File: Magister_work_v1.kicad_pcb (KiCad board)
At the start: 4 copper layers, 100 x 100 mm, 83 parts, among them J1 Conn_01x04_Pin, J10 Conn_01x02_Pin, J2 Conn_01x03_Pin, J3 Conn_01x03_Pin, J4 Conn_01x03_Pin, J5 Conn_01x03_Pin, J6 Conn_01x04_Pin, J7 Conn_01x04_Pin, J8 Conn_01x06_Pin, J9 Conn_01x02_Pin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

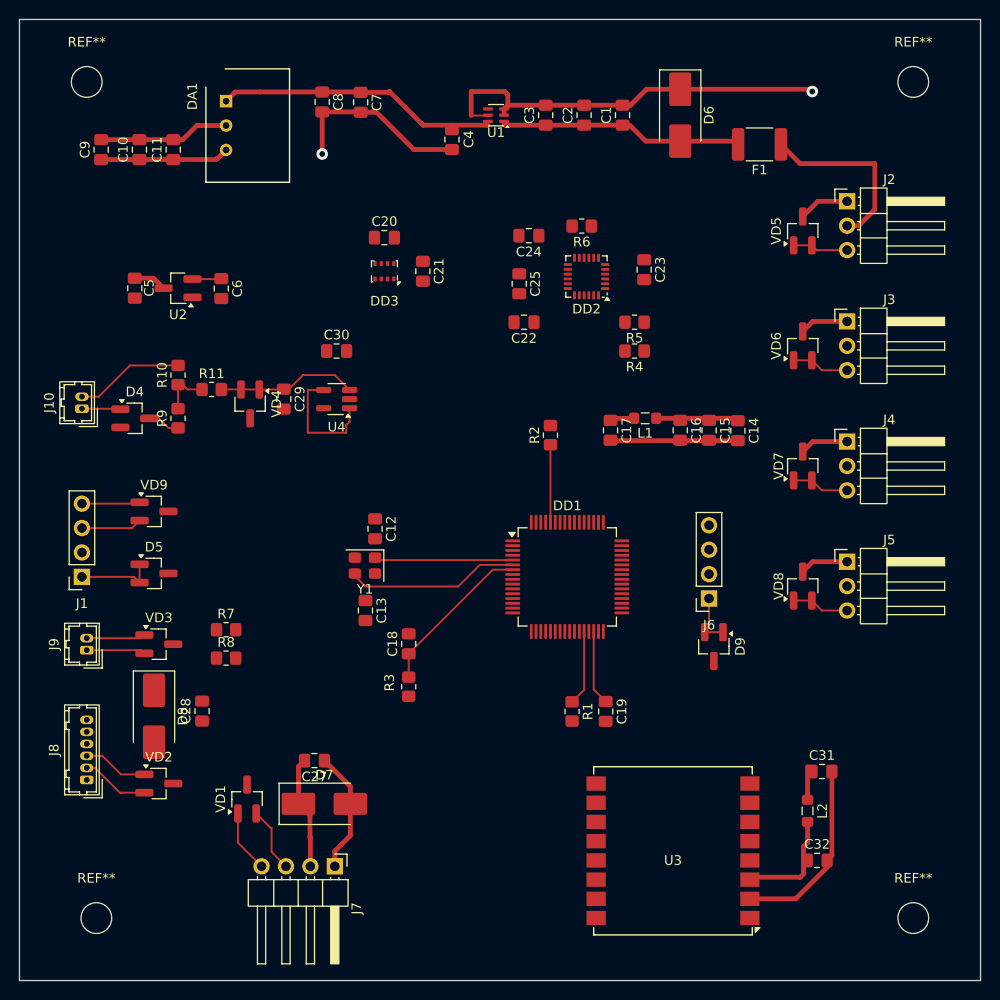
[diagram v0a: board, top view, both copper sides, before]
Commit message: feat: added power lines for MCU
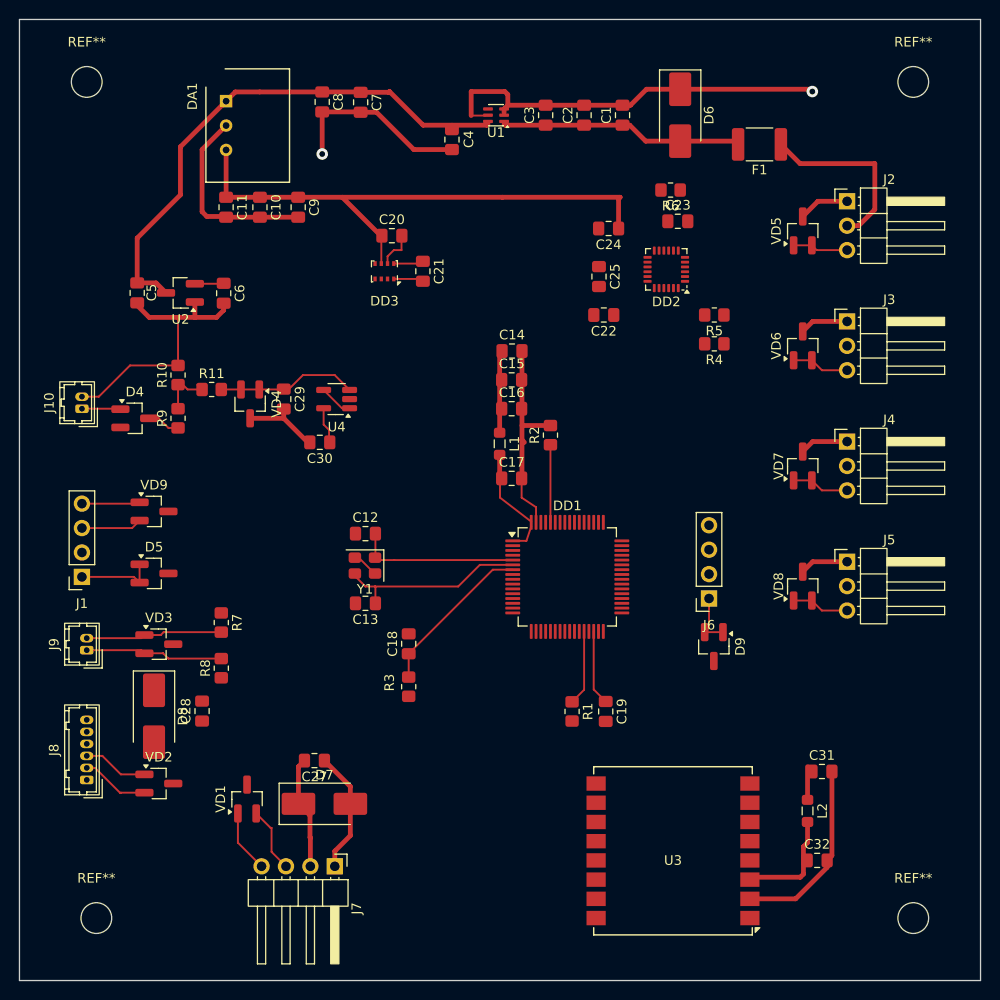
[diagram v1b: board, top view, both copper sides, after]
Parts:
- moved C14 24.9 mm to (76.2, 59.5), turned to 0 degrees
- moved C9 21.4 mm to (54.0, 44.5), turned to -90 degrees
- moved C15 21.2 mm to (76.2, 62.5), turned to 0 degrees
- moved C16 17.7 mm to (76.2, 65.5), turned to 0 degrees
- moved L1 15.4 mm to (75.0, 69.2), turned to -90 degrees
- moved C10 13.9 mm to (50.0, 44.5), turned to -90 degrees
- moved C17 11.4 mm to (76.2, 72.8), turned to 0 degrees
- moved R6 9.98 mm to (92.8, 42.8)
- moved C30 9.66 mm to (56.2, 69.0), turned to 180 degrees
- moved C22 8.33 mm to (85.8, 55.8)
- moved C24 8.33 mm to (86.3, 46.8)
- moved C25 8.33 mm to (85.3, 51.8)
- moved DD2 8.33 mm to (92.3, 51.0)
- moved R4 8.33 mm to (97.3, 58.8)
- moved R5 8.33 mm to (97.3, 55.8)
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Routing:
- net GND: track 227.1 -> 272.5 mm
- net +3V3D: track 25.5 -> 70.0 mm
- net +5V: track 45.4 -> 68.2 mm
- net BAT_CTRL: track 12.8 -> 3.49 mm
- net BN_880_SDA: track 6.13 -> 14.4 mm
- net BN_880_SCL: track 6.13 -> 14.3 mm
- net +3V3A: track 3.02 -> 9.93 mm
- net Net-(DD1-PH0): track 14.4 -> 16.9 mm
- net Net-(DD1-PH1): track 18.1 -> 19.8 mm

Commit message: fix: fix bug with locked hole
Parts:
- removed REF** (x4): MountingHole_3.2mm_M3, MountingHole:MountingHole_3.2mm_M3
- added ?: , , F.Cu at (118.0, 31.5)
- added ?: , , F.Cu at (118.0, 118.5)
- added ?: , , F.Cu at (32.0, 31.5)
- added ?: , , F.Cu at (33.0, 118.5)
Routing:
- net GND: track 272.5 -> 286.2 mm
- net +5V: track 68.2 -> 76.8 mm, vias 0 -> 1

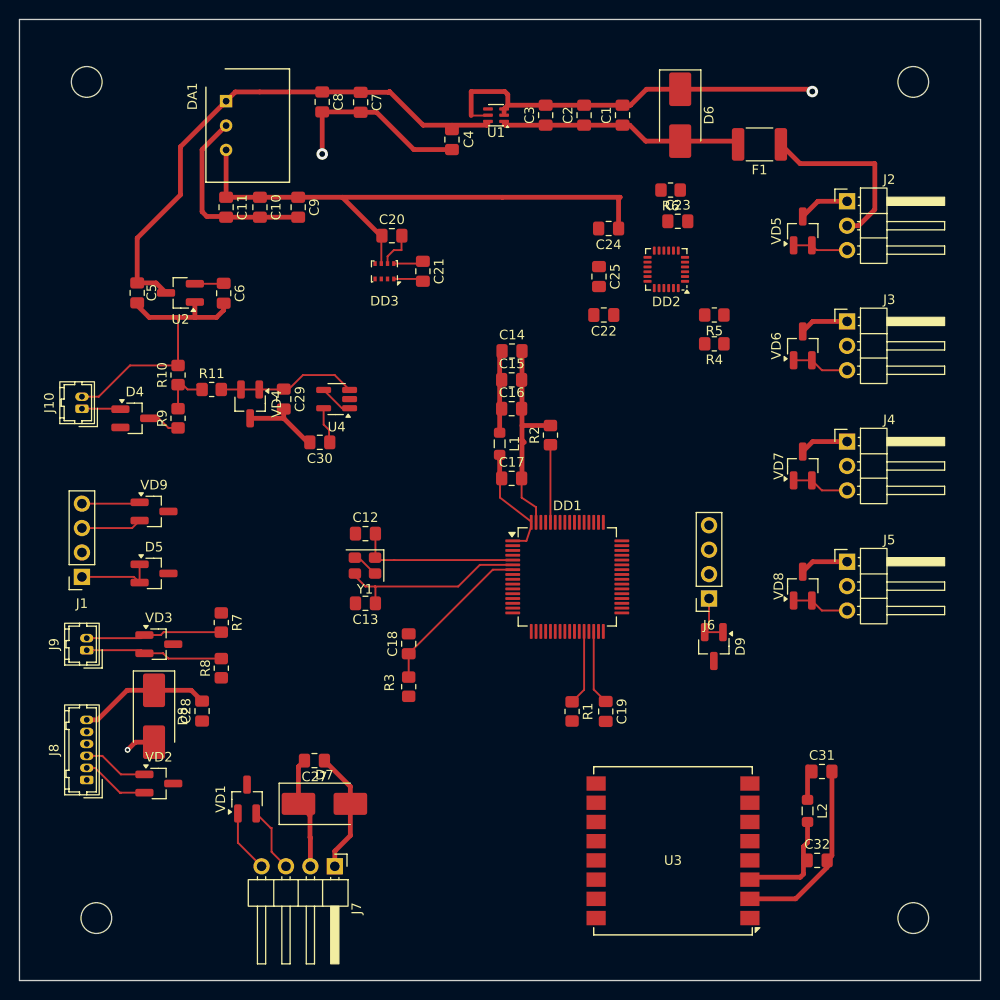
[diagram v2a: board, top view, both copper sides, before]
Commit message: feat: added MPU and PWM line
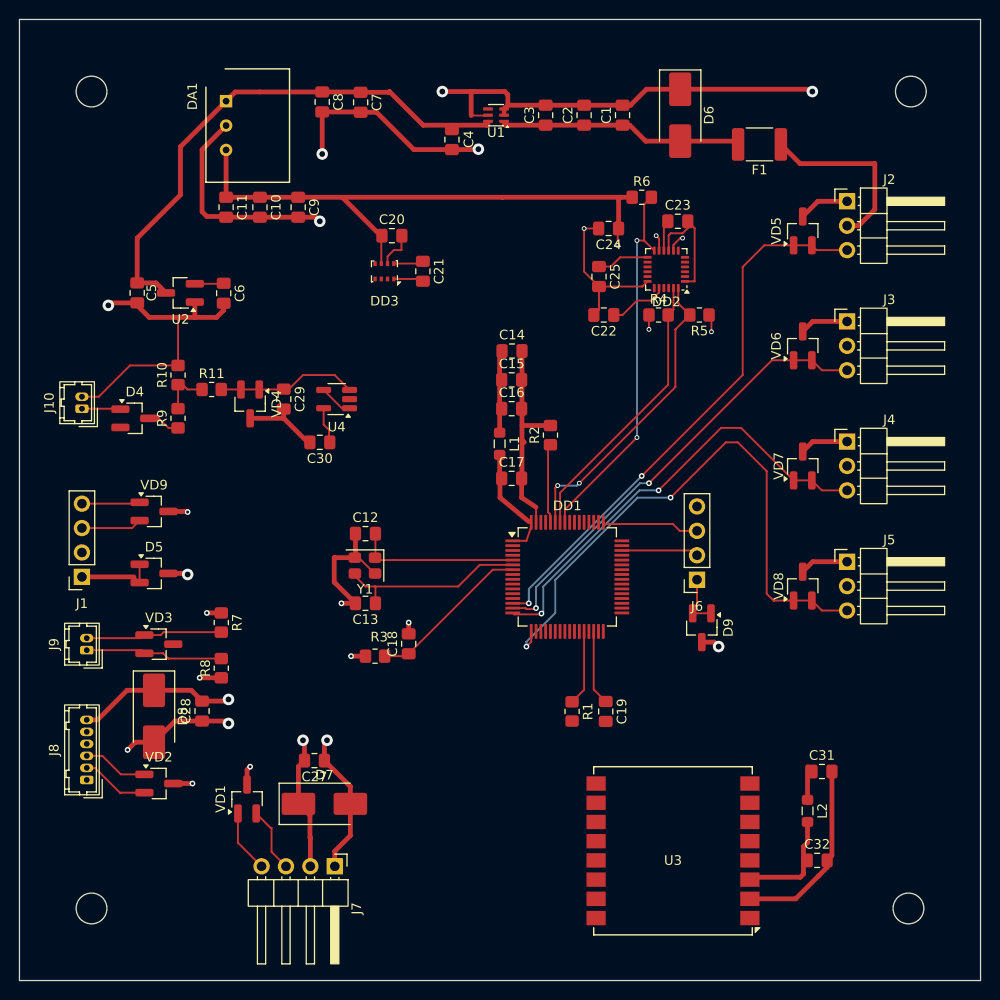
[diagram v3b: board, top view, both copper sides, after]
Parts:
- moved R4 6.53 mm to (91.5, 55.8), turned to 0 degrees
- moved R3 4.73 mm to (62.0, 91.2), turned to 0 degrees
- moved R6 3.09 mm to (89.8, 43.5), turned to 0 degrees
- moved D9 2.32 mm to (96.0, 88.3)
- moved J6 2.32 mm to (95.5, 83.3)
- moved R5 1.55 mm to (95.8, 55.8)
- moved ? 1.12 mm to (117.5, 117.5)
- moved ? 1.12 mm to (32.5, 32.5)
- moved ? 1.12 mm to (32.5, 117.5)
- moved ? 1.03 mm to (117.8, 32.5)
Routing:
- net GND: track 286.2 -> 395.7 mm, vias 2 -> 15
- net PWM4: track 6.00 -> 61.0 mm, vias 0 -> 2
- net PWM1: track 5.77 -> 57.9 mm, vias 0 -> 2
- net PWM2: track 6.00 -> 47.3 mm, vias 0 -> 2
- net PWM3: track 6.00 -> 47.1 mm, vias 0 -> 2
- net INT_MPU6050: track 0.00 -> 39.5 mm, vias 0 -> 2
- net +3V3D: track 70.0 -> 108.4 mm, vias 0 -> 8
- net SDA_MPU6050: track 0.00 -> 31.8 mm, vias 0 -> 2
- net SCL_MPU6050: track 0.00 -> 29.3 mm
- net +5V: track 76.8 -> 89.8 mm, vias 1 -> 4
- net Net-(DD1-PA14): track 0.00 -> 10.1 mm
- net Net-(DD1-PA13): track 0.00 -> 8.03 mm
- net Net-(DD2-CPOUT): track 0.00 -> 6.14 mm
- net +3V3A: track 9.93 -> 15.4 mm
- net Net-(DD2-REGOUT): track 0.00 -> 3.22 mm

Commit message: feat: added mani lines for GND
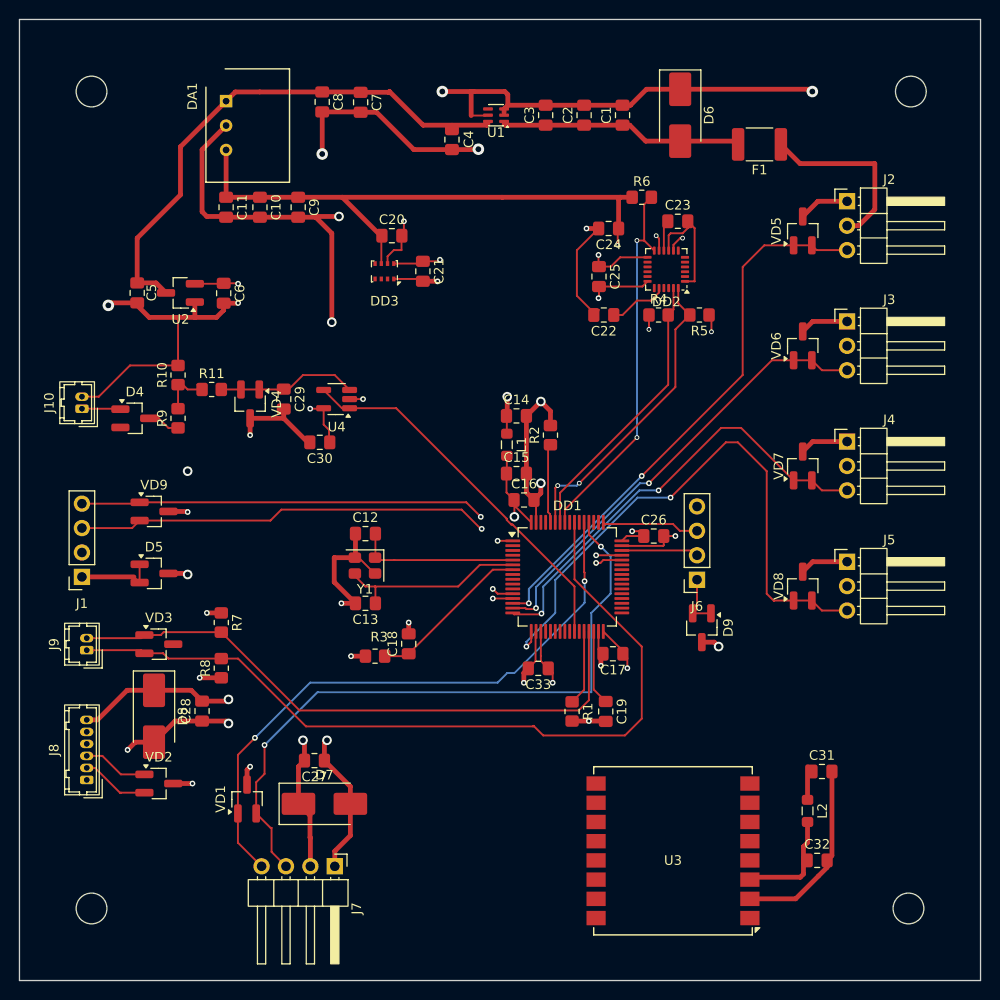
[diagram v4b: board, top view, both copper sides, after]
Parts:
- added C26: 0.1u, Capacitor_SMD:C_0805_2012Metric_Pad1.18x1.45mm_HandSolder, F.Cu at (91.0, 78.8)
- added C33: 0.1u, Capacitor_SMD:C_0805_2012Metric_Pad1.18x1.45mm_HandSolder, F.Cu at (79.0, 92.5)
- moved C17 21.1 mm to (86.8, 91.0), turned to 180 degrees
- moved C15 9.76 mm to (76.7, 72.2)
- moved C16 9.59 mm to (77.5, 75.0)
- moved C14 6.77 mm to (76.7, 66.2)
- moved L1 0.76 mm to (75.7, 69.2)
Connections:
- C15 pad 1: +3V3D -> +3V3_MCU
- C16 pad 1: +3V3D -> +3V3_MCU
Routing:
- net GND: track 395.7 -> 655.5 mm, vias 15 -> 30
- net +3V3A: track 15.4 -> 123.1 mm, vias 0 -> 5
- net +3V3_MCU: track 2.71 -> 76.9 mm, vias 0 -> 5
- net BN_880_SDA: track 14.4 -> 85.5 mm
- net HC_trigger: track 6.84 -> 70.0 mm, vias 0 -> 2
- net HC_echo: track 6.52 -> 63.6 mm, vias 0 -> 2
- net TX_debug: track 6.32 -> 59.4 mm, vias 0 -> 2
- net RX_debug: track 6.06 -> 58.5 mm, vias 0 -> 2
- net BN_880_SCL: track 14.3 -> 63.5 mm
- net BAT_CTRL: track 3.49 -> 39.3 mm
- net +3V3D: track 108.4 -> 103.7 mm, vias 8 -> 9

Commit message: feat: add zone for 3v3D power
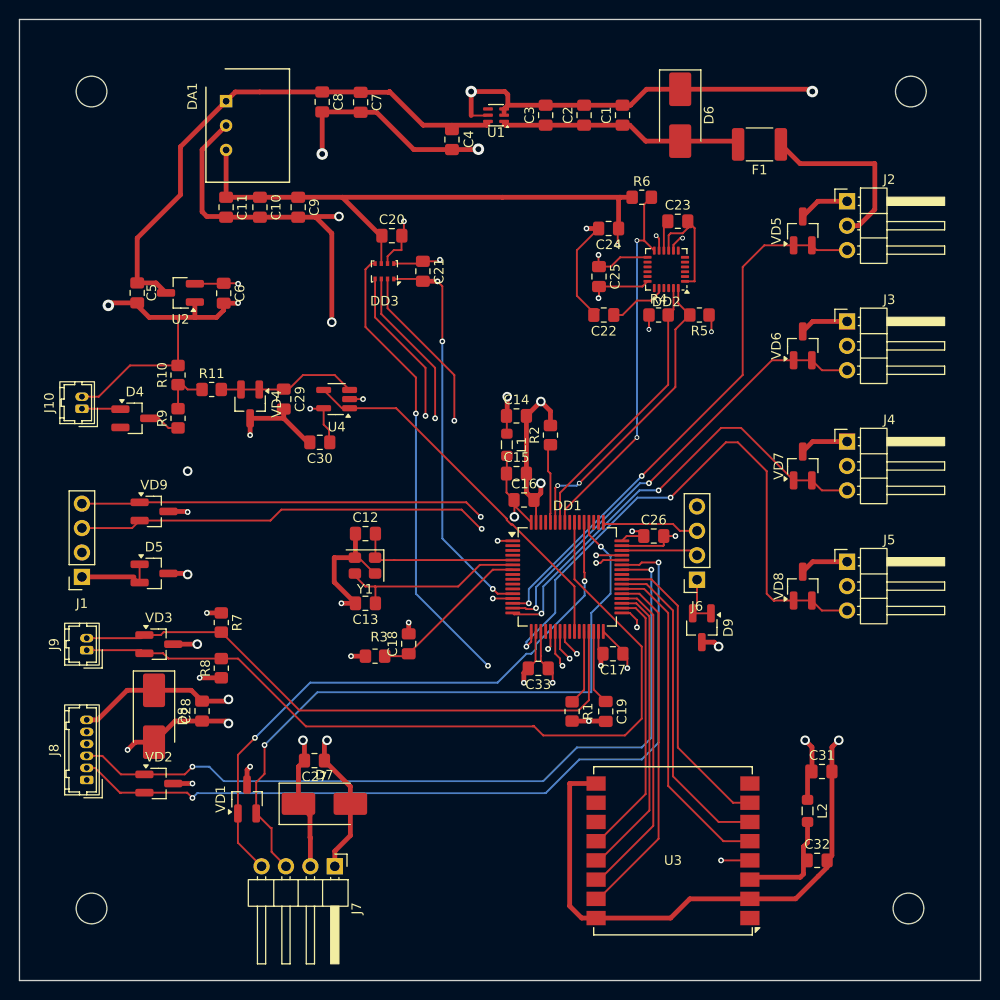
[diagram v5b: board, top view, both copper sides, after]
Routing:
- net +5V: track 89.8 -> 183.9 mm
- net BN_880_TX: track 7.11 -> 85.9 mm, vias 0 -> 2
- net BN_880_RX: track 6.80 -> 82.9 mm, vias 0 -> 2
- net GND: track 655.5 -> 727.1 mm, vias 30 -> 33
- net SDO_BMP280: track 0.00 -> 64.1 mm, vias 0 -> 3
- net SDI_BMP280: track 0.00 -> 53.8 mm, vias 0 -> 2
- net CSB_BMP280: track 0.00 -> 53.2 mm, vias 0 -> 2
- net SCK_BMP280: track 0.00 -> 51.2 mm, vias 0 -> 2
- net +3V3_MCU: track 76.9 -> 27.4 mm
- net SS_LoRa: track 0.00 -> 37.2 mm
- net DIO0_LoRa: track 0.00 -> 34.7 mm
- net MOSI_LoRa: track 0.00 -> 34.2 mm
- net DIO1_LoRa: track 0.00 -> 33.7 mm
- net Reset_LoRa: track 0.00 -> 33.5 mm, vias 0 -> 2
- net DIO2_LoRa: track 0.00 -> 31.6 mm
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- added copper zone on In1.Cu, net +3V3D
- added copper zone on In1.Cu, net +3V3_MCU
- added copper zone on In1.Cu, net +5V

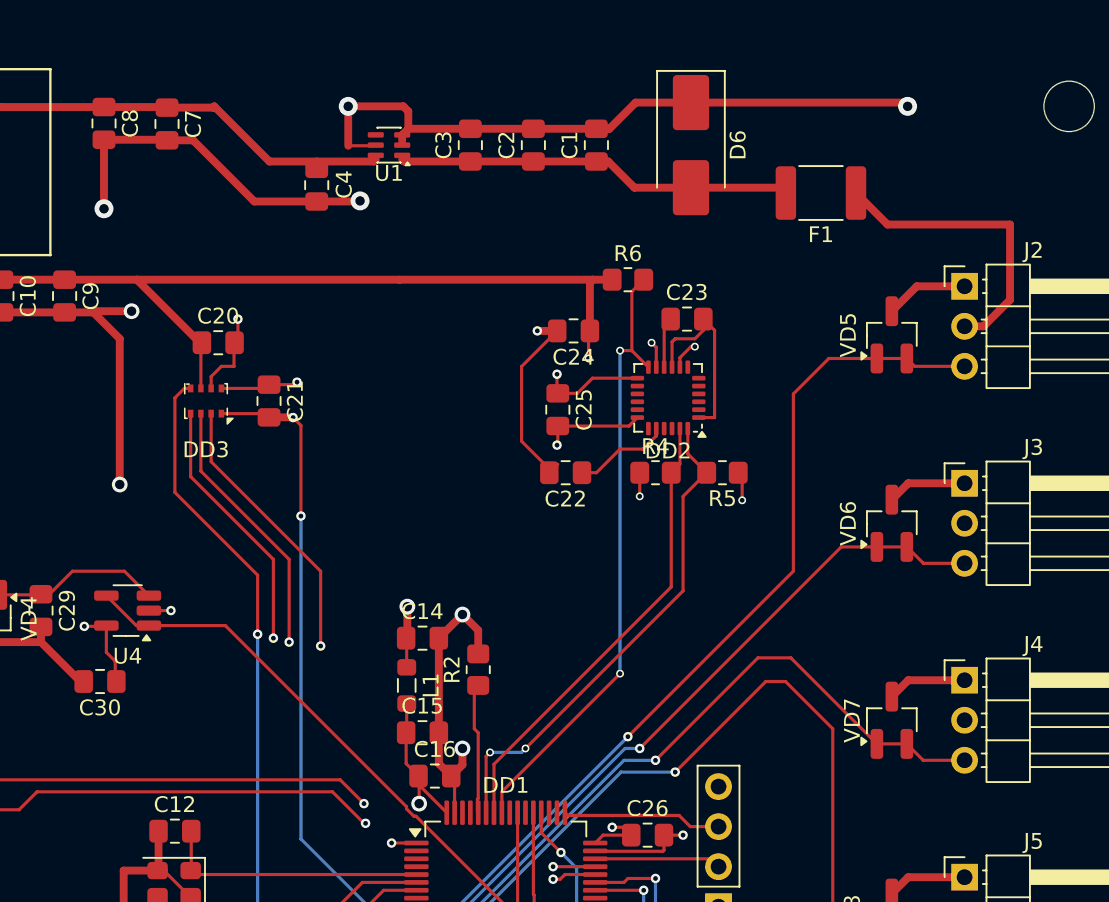
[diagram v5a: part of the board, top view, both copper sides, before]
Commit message: feat: added zone for GND and 3v3A
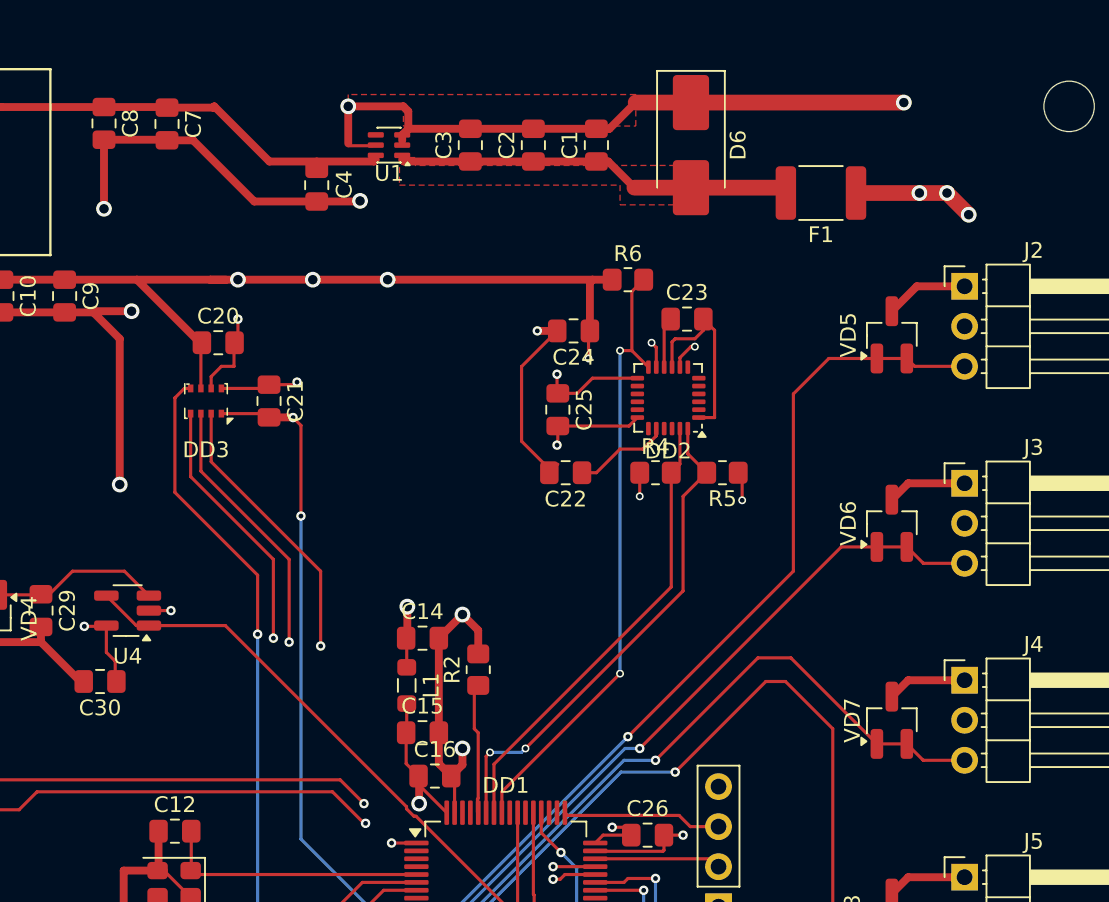
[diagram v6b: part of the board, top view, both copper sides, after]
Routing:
- net +3V3D: track 107.2 -> 108.2 mm, vias 10 -> 13
- net GND: track 727.1 -> 726.4 mm
- net +5V_1: track 68.4 -> 69.0 mm, vias 0 -> 3
- added copper zone on In1.Cu, net +5V_1
- added copper zone on F.Cu, net +5V_2
- added copper zone on F.Cu, net GND
- added copper zone on In2.Cu, net GND

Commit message: feat: first version complitr PCB
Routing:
- net GND: track 726.4 -> 742.0 mm, vias 33 -> 43
- net +3V3D: track 108.2 -> 109.0 mm
- added copper zone on F.Cu, net +5V
